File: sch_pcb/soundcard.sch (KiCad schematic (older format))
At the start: 77 parts, among them J501 MicroUSB, Q501 BSR315PH6327XTSA1, U501 CM108B, U502 CM108B, U503 TUSB2036, U504 MCP1703A-3302/MB, U505 CM108B, Y501 6MHz

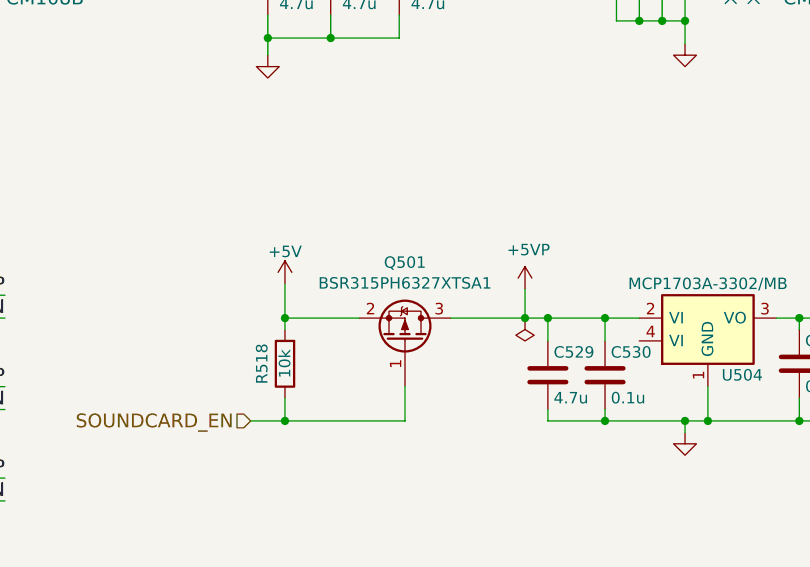
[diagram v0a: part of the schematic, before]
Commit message: Add Digikey part # to all parts.  Fix unconnected nets
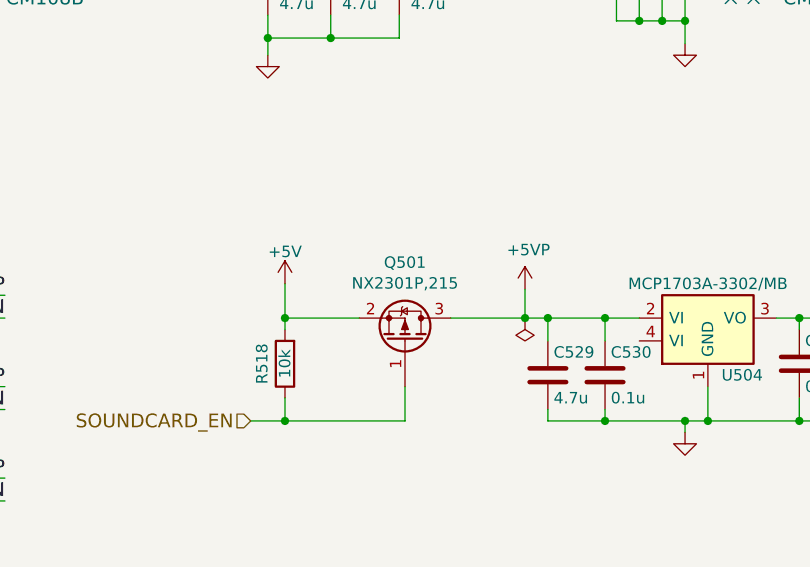
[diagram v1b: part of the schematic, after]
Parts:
- C501, C503, C505, C507, C513, C514, C515, C516, C517, C518, C519, C520, C529, C532, C533, C534, C535, C537, C538, C539: Digikey PN (none) -> 1276-2087-1-ND
- C502, C504, C506, C508, C521, C522, C530, C531, C543: Digikey PN (none) -> 399-1096-1-ND
- C509, C510, C511, C512, C527, C528, C540, C541, C542: Digikey PN (none) -> 478-5165-1-ND
- C523, C524, C525, C526: Digikey PN (none) -> 399-1054-1-ND
- J501: Digikey PN (none) -> 609-4613-1ND
- Q501: value BSR315PH6327XTSA1 -> NX2301P,215; Digikey PN (none) -> 1727-1148-1-ND
- R501, R509, R510, R511, R512, R513, R517, R521, R522: Digikey PN (none) -> 311-15KGRCT-ND
- R502, R514: Digikey PN (none) -> 311-1.5KGRCT-ND
- R503, R504, R505, R506, R507, R508, R519, R520: Digikey PN (none) -> 311-22GRCT-ND
- R515, R516, R523: Digikey PN (none) -> 311-33GRCT-ND
- R518: Digikey PN (none) -> 311-10KGRCT-ND
- U501, U502, U505: Digikey PN (none) -> symmetry
- U503: Digikey PN (none) -> 296-27129-1-ND
- U504: Digikey PN (none) -> MCP1700T3302EMBCT-ND

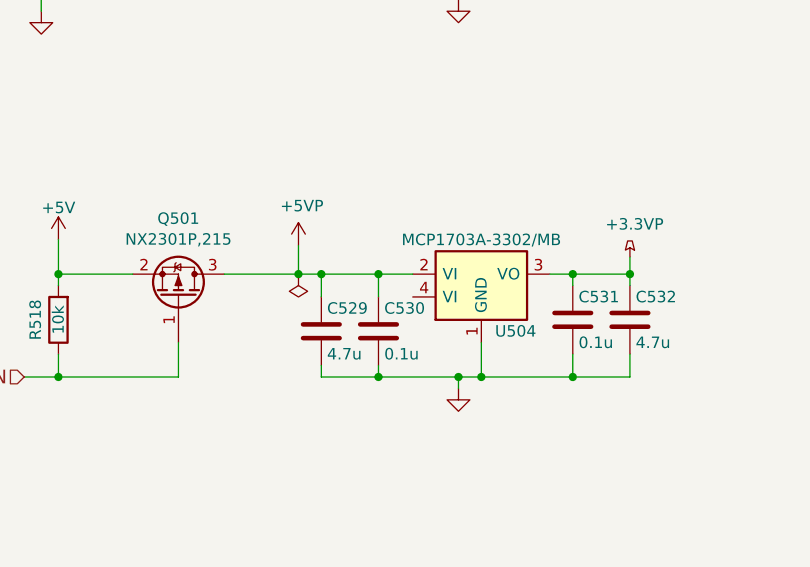
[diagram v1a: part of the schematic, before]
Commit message: Switch to 0402 parts and SeeedStudio footprints
Silk screen is still being updated.  BOM needs to be updated as well
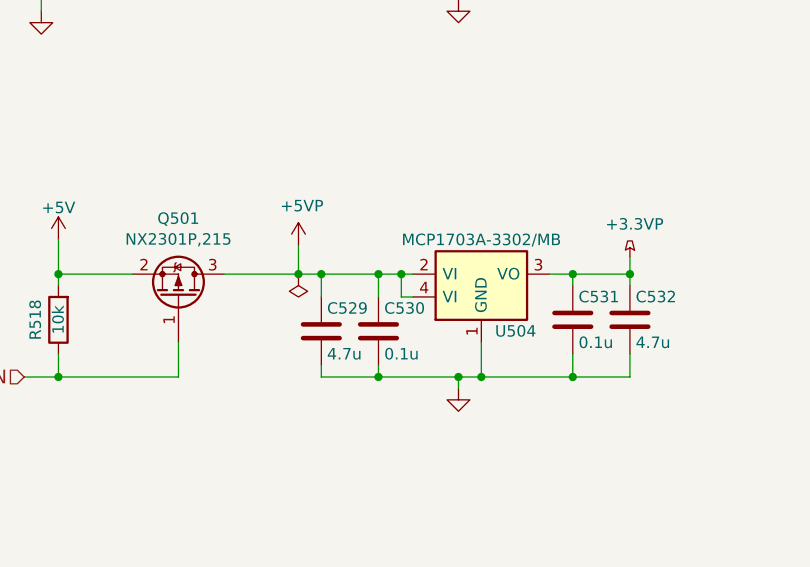
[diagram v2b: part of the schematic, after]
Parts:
- C501, C502, C503, C504, C505, C506, C507, C508, C513, C514, C515, C516, C517, C518, C519, C520, C521, C522, C523, C524, C525, C526, C529, C530, C531, C532, C533, C534, C535, C536, C537, C538, C539, C543: footprint lib:smd0603 -> lib:OPL_C0402
- C509, C510, C511, C512, C527, C528, C540, C541, C542: footprint lib:smd0805 -> lib:OPL_C0603
- J501: footprint lib:USB_Micro-B -> lib:OPL_MICRO-USB5+4P-SMD-0.65-B
- Q501: footprint lib:SOT23 -> lib:OPL_SOT-23
- R501, R502, R503, R504, R505, R506, R507, R508, R509, R510, R511, R512, R513, R514, R515, R516, R517, R518, R519, R520, R521, R522, R523: footprint lib:smd0603 -> lib:OPL_R0402
- U504: footprint lib:sot89 -> lib:OPL_SOT-89
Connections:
- net +5VP: now also U504.4 (VI)
